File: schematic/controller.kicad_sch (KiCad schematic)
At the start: 7 parts, among them U18 74LS541, U19 74LS541

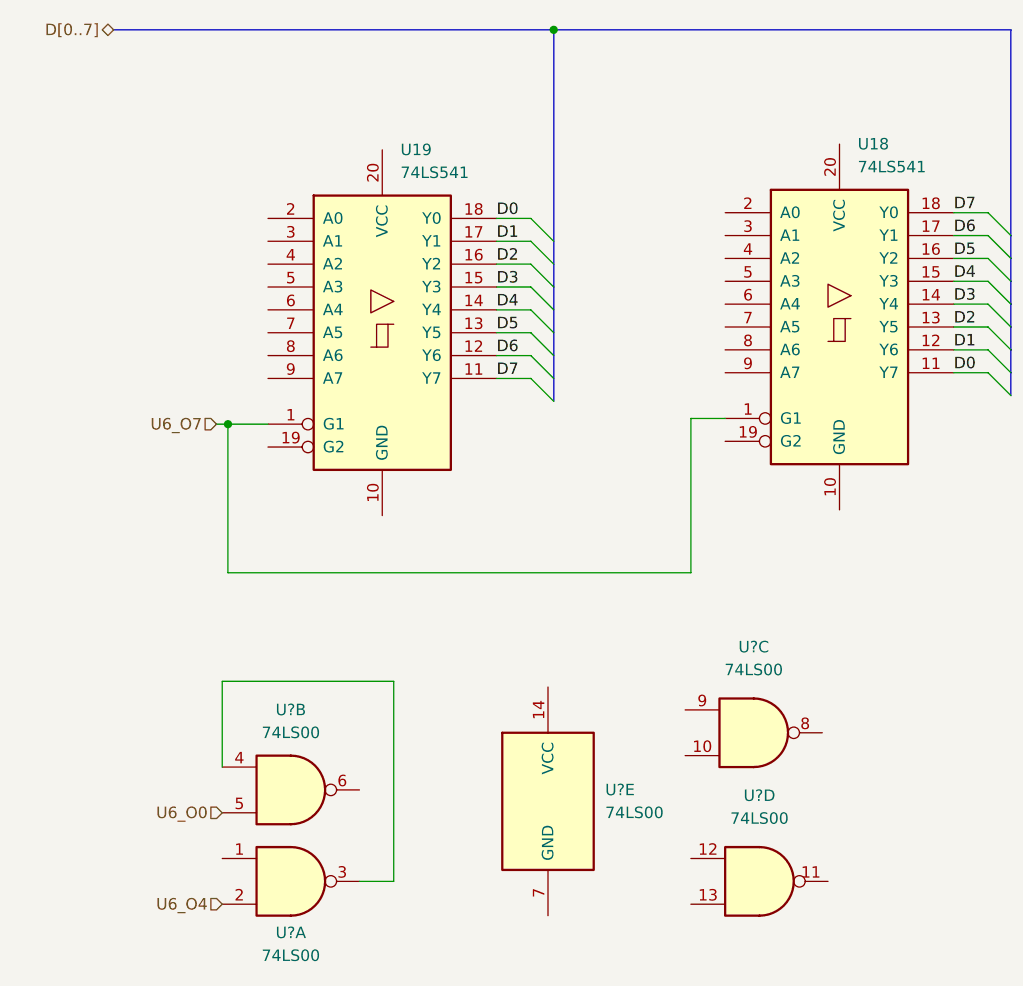
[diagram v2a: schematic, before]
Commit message: completed sound block, finished cart io port, and finished decoder.
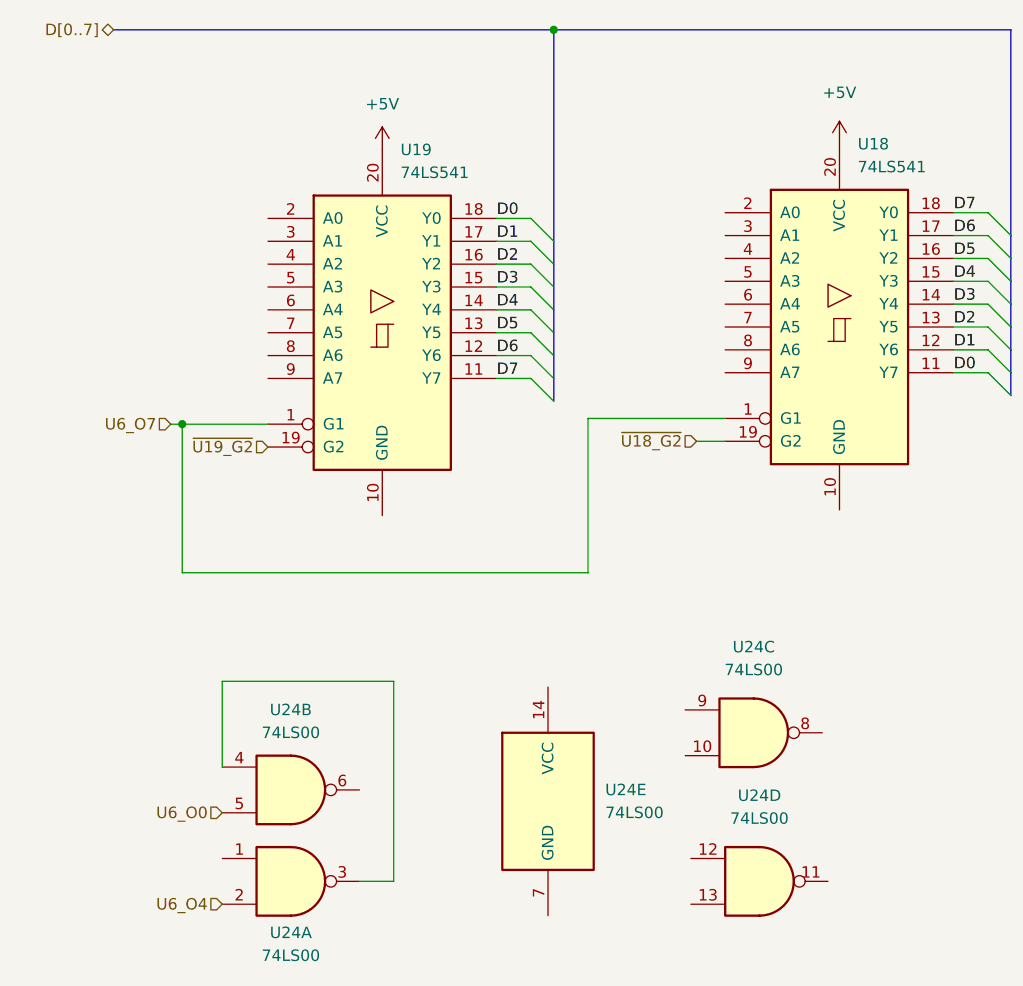
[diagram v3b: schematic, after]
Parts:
- gave numbers to parts that had none: 1
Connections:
- net ~{U19_G2}: now reaches U19.19 (G2)
- net +5V: now reaches U19.20 (VCC)
- net +5V: now also U18.20 (VCC)
- net ~{U18_G2}: now reaches U18.19 (G2)
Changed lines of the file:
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@@
 (kicad_sch (version 20211123) (generator eeschema)
   (paper "A4")
-  (junction (at 106.68 97.79) (diameter 0) (color 0 0 0 0)
+  (junction (at 101.6 97.79) (diameter 0) (color 0 0 0 0)
   )
   (junction (at 142.875 53.975) (diameter 0) (color 0 0 0 0)
@@
     (stroke (width 0) (type default) (color 0 0 0 0))
   )
-  (wire (pts (xy 106.68 97.79) (xy 106.68 114.3))
+  (wire (pts (xy 101.6 97.79) (xy 101.6 114.3))
     (stroke (width 0) (type default) (color 0 0 0 0))
   )
@@
     (stroke (width 0) (type default) (color 0 0 0 0))
   )
-  (wire (pts (xy 106.68 97.79) (xy 111.125 97.79))
+  (wire (pts (xy 101.6 97.79) (xy 111.125 97.79))
+    (stroke (width 0) (type default) (color 0 0 0 0))
+  )
+  (wire (pts (xy 158.75 99.695) (xy 161.925 99.695))
     (stroke (width 0) (type default) (color 0 0 0 0))
   )
@@
     (stroke (width 0) (type default) (color 0 0 0 0))
   )
-  (wire (pts (xy 106.68 114.3) (xy 158.115 114.3))
+  (wire (pts (xy 101.6 114.3) (xy 146.685 114.3))
     (stroke (width 0) (type default) (color 0 0 0 0))
   )
@@
     (stroke (width 0) (type default) (color 0 0 0 0))
   )
-  (wire (pts (xy 158.115 97.155) (xy 161.925 97.155))
+  (wire (pts (xy 146.685 97.155) (xy 161.925 97.155))
     (stroke (width 0) (type default) (color 0 0 0 0))
   )
@@
     (stroke (width 0) (type default) (color 0 0 0 0))
   )
-  (wire (pts (xy 105.41 97.79) (xy 106.68 97.79))
+  (wire (pts (xy 100.33 97.79) (xy 101.6 97.79))
     (stroke (width 0) (type default) (color 0 0 0 0))
   )
@@
     (stroke (width 0) (type default) (color 0 0 0 0))
   )
-  (wire (pts (xy 158.115 114.3) (xy 158.115 97.155))
+  (wire (pts (xy 146.685 114.3) (xy 146.685 97.155))
     (stroke (width 0) (type default) (color 0 0 0 0))
   )
@@
     (effects (font (size 1.27 1.27)) (justify right))
   )
-  (hierarchical_label "U6_O7" (shape input) (at 105.41 97.79 180)
+  (hierarchical_label "U6_O7" (shape input) (at 100.33 97.79 180)
+    (effects (font (size 1.27 1.27)) (justify right))
+  )
+  (hierarchical_label "~{U19_G2}" (shape input) (at 111.125 100.33 180)
     (effects (font (size 1.27 1.27)) (justify right))
   )
   (hierarchical_label "D[0..7]" (shape bidirectional) (at 93.98 53.975 180)
+    (effects (font (size 1.27 1.27)) (justify right))
+  )
+  (hierarchical_label "~{U18_G2}" (shape input) (at 158.75 99.695 180)
     (effects (font (size 1.27 1.27)) (justify right))
   )
@@
   (symbol (lib_id "74xx:74LS00") (at 165.735 148.59 0) (unit 4)
     (in_bom yes) (on_board yes) (fields_autoplaced)
-    (property "Reference" "U?" (id 0) (at 165.735 139.065 0))
+    (property "Reference" "U24" (id 0) (at 165.735 139.065 0))
     (property "Value" "74LS00" (id 1) (at 165.735 141.605 0))
     (property "Footprint" "" (id 2) (at 165.735 148.59 0)
@@
   (symbol (lib_id "74xx:74LS00") (at 142.24 139.7 0) (unit 5)
     (in_bom yes) (on_board yes) (fields_autoplaced)
-    (property "Reference" "U?" (id 0) (at 148.59 138.4299 0)
+    (property "Reference" "U24" (id 0) (at 148.59 138.4299 0)
       (effects (font (size 1.27 1.27)) (justify left))
     )
@@
     (pin "7")
   )
+  (symbol (lib_id "power:+5V") (at 123.825 67.31 0) (unit 1)
+    (in_bom yes) (on_board yes) (fields_autoplaced)
+    (property "Reference" "#PWR?" (id 0) (at 123.825 71.12 0)
+      (effects (font (size 1.27 1.27)) hide)
+    )
+    (property "Value" "+5V" (id 1) (at 123.825 62.23 0))
+    (property "Footprint" "" (id 2) (at 123.825 67.31 0)
+      (effects (font (size 1.27 1.27)) hide)
+    )
+    (property "Datasheet" "" (id 3) (at 123.825 67.31 0)
+      (effects (font (size 1.27 1.27)) hide)
+    )
+    (pin "1")
+  )
   (symbol (lib_id "74xx:74LS00") (at 165.1 132.08 0) (unit 3)
     (in_bom yes) (on_board yes) (fields_autoplaced)
-    (property "Reference" "U?" (id 0) (at 165.1 122.555 0))
+    (property "Reference" "U24" (id 0) (at 165.1 122.555 0))
     (property "Value" "74LS00" (id 1) (at 165.1 125.095 0))
     (property "Footprint" "" (id 2) (at 165.1 132.08 0)
@@
     (pin "7")
   )
+  (symbol (lib_id "power:+5V") (at 174.625 66.675 0) (unit 1)
+    (in_bom yes) (on_board yes) (fields_autoplaced)
+    (property "Reference" "#PWR?" (id 0) (at 174.625 70.485 0)
+      (effects (font (size 1.27 1.27)) hide)
+    )
+    (property "Value" "+5V" (id 1) (at 174.625 60.96 0))
+    (property "Footprint" "" (id 2) (at 174.625 66.675 0)
+      (effects (font (size 1.27 1.27)) hide)
+    )
+    (property "Datasheet" "" (id 3) (at 174.625 66.675 0)
+      (effects (font (size 1.27 1.27)) hide)
+    )
+    (pin "1")
+  )
   (symbol (lib_id "74xx:74LS00") (at 113.665 148.59 0) (unit 1)
     (in_bom yes) (on_board yes)
-    (property "Reference" "U?" (id 0) (at 113.665 154.305 0))
+    (property "Reference" "U24" (id 0) (at 113.665 154.305 0))
     (property "Value" "74LS00" (id 1) (at 113.665 156.845 0))
     (property "Footprint" "" (id 2) (at 113.665 148.59 0)
@@
   (symbol (lib_id "74xx:74LS00") (at 113.665 138.43 0) (unit 2)
     (in_bom yes) (on_board yes) (fields_autoplaced)
-    (property "Reference" "U?" (id 0) (at 113.665 129.54 0))
+    (property "Reference" "U24" (id 0) (at 113.665 129.54 0))
     (property "Value" "74LS00" (id 1) (at 113.665 132.08 0))
     (property "Footprint" "" (id 2) (at 113.665 138.43 0)

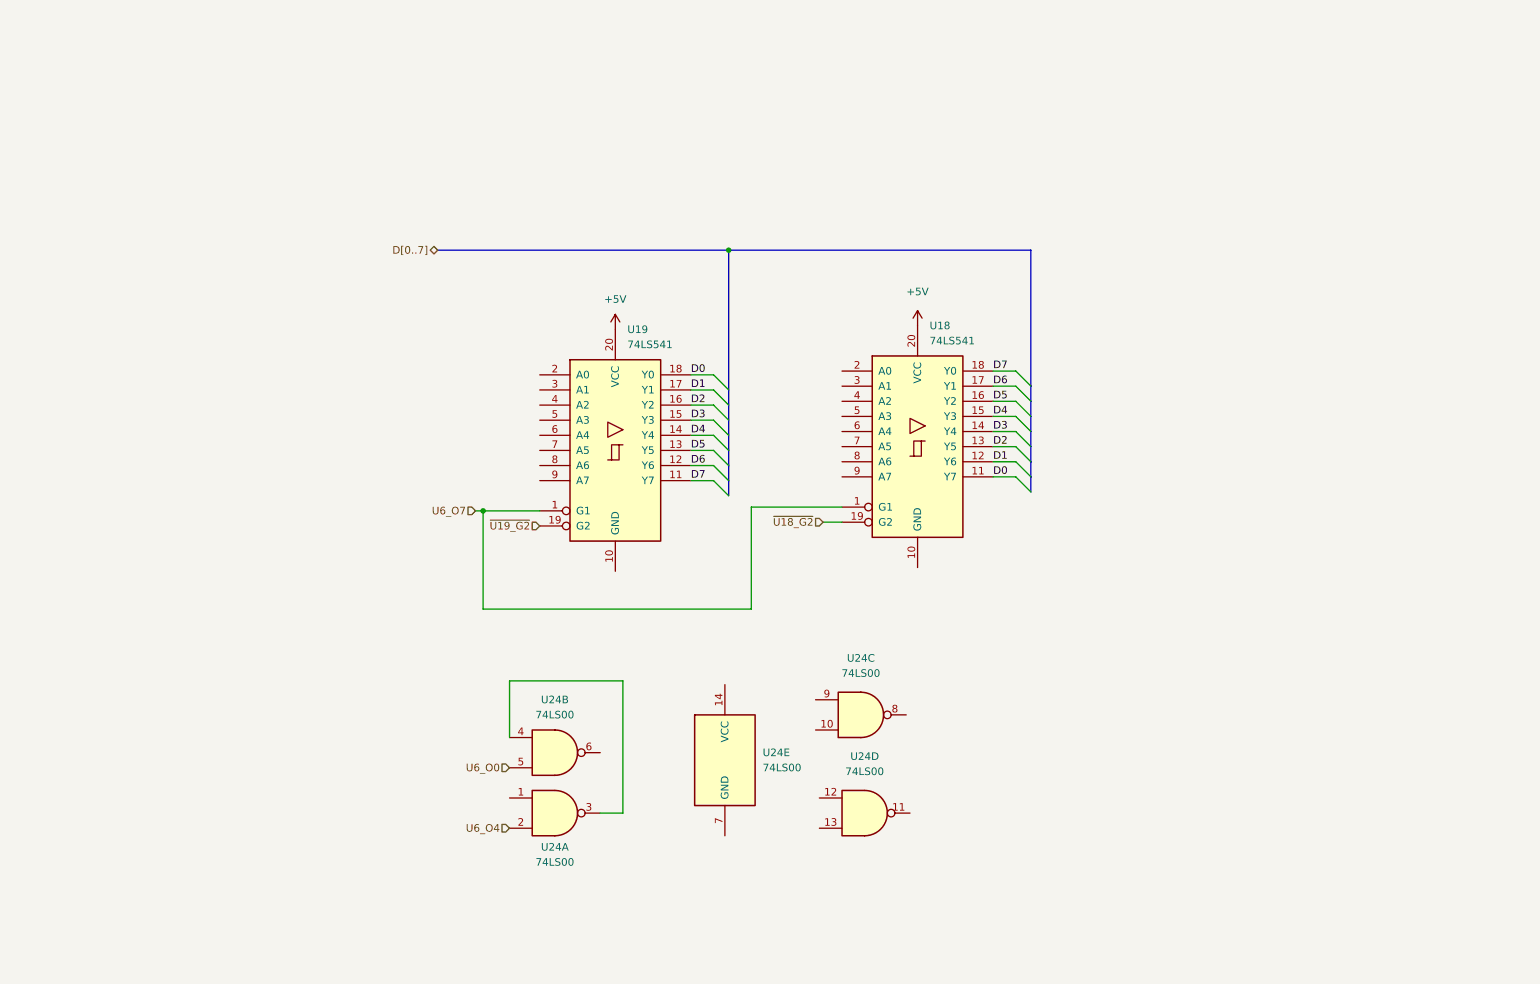
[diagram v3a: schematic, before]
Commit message: power supply added, controller circuit added. Controller is a very odd duck to say the least. Seems they wanted to have plenty of current, maybe due to the steering wheel attachement?
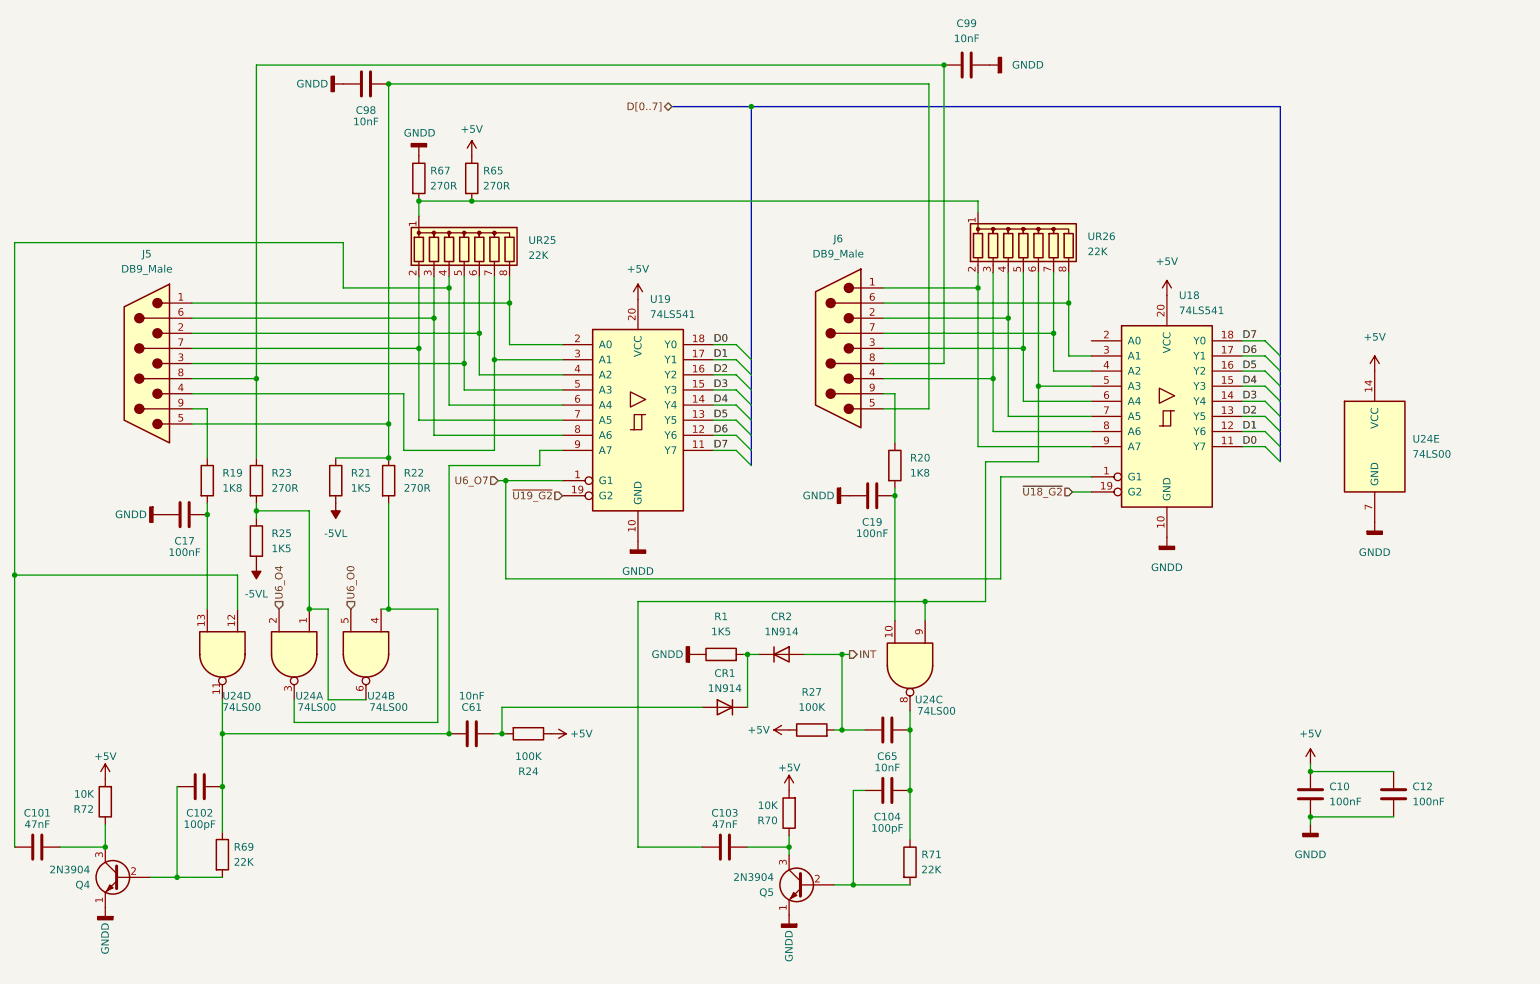
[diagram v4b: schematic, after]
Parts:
- added C10, C12, C17, C19: 100nF, symbol Device:C
- added C101, C103: 47nF, symbol Device:C
- added C102, C104: 100pF, symbol Device:C
- added C61, C65, C98, C99: 10nF, symbol Device:C
- added CR1, CR2: 1N914, symbol Device:D
- added J5, J6: DB9_Male, symbol Connector:DB9_Male
- added Q4, Q5: 2N3904, Package_TO_SOT_THT:TO-92_Inline, symbol Transistor_BJT:2N3904
- added R1, R21, R25: 1K5, symbol Device:R
- added R19, R20: 1K8, symbol Device:R
- added R22, R23, R65, R67: 270R, symbol Device:R
- added R24, R27: 100K, symbol Device:R
- added R69, R71: 22K, symbol Device:R
- added R70, R72: 10K, symbol Device:R
- added UR25, UR26: 22K, Resistor_THT:R_Array_SIP8, symbol Device:R_Network07
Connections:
- net +5V: now also U24.14 (VCC), C10.1, C12.1, R24.1, R27.1, R65.1, R70.2, R72.2
- net GNDD: now reaches U19.10 (GND)
- net GNDD: now also U18.10 (GND), U24.7 (GND), C10.2, C12.2, C17.1, C19.1, C98.1, C99.2, Q4.1 (E), Q5.1 (E), R1.1, R67.1
- net at U19.2 (A0): now also J5.1, UR25.8 (R7)
- net at U19.3 (A1): now also J5.4, UR25.7 (R6)
- net at U19.4 (A2): now also J5.2, UR25.6 (R5)
- net at U19.5 (A3): now also J5.3, UR25.5 (R4)
- net at U19.6 (A4): now also U24.12, C101.2, UR25.4 (R3)
- net at U19.7 (A5): now also J5.7, UR25.2 (R1)
- net at U19.8 (A6): now also J5.6, UR25.3 (R2)
- net at U19.9 (A7): now also U24.11, C102.2, C61.2, R69.1
- net at U24.13: now also C17.2, R19.2
- net at U18.3 (A1): now also J6.6, UR26.8 (R7)
- net at U18.4 (A2): now also J6.7, UR26.7 (R6)
- net at U18.5 (A3): now also U24.9, C103.2, UR26.6 (R5)
- net at U18.6 (A4): now also J6.3, UR26.5 (R4)
- net at U18.7 (A5): now also J6.2, UR26.4 (R3)
- net at U18.8 (A6): now also J6.4, UR26.3 (R2)
- net at U18.9 (A7): now also J6.1, UR26.2 (R1)
- net at U24.10: now also C19.2, R20.2
- net at U24.8: now also C104.2, C65.2, R71.1
- net at U24.1: now also U24.6, R23.2, R25.1
- net at U24.3, U24.4: now also R22.2
- new net: CR1.1 (K), CR2.1 (K), R1.2
- new net: R65.2, R67.2, UR25.1 (common), UR26.1 (common)
- new net: C102.1, Q4.2 (B), R69.2
- new net: C101.1, Q4.3 (C), R72.1
- new net: C98.2, J5.5, J6.5, R21.1, R22.1
- new net: C61.1, CR1.2 (A), R24.2
- new net: C99.1, J5.8, J6.8, R23.1
- new net: C104.1, Q5.2 (B), R71.2
- new net: C103.1, Q5.3 (C), R70.1
- new net: J5.9, R19.1
- new net: J6.9, R20.1
- new net -5VL: R21.2, R25.2
- new net INT: C65.1, CR2.2 (A), R27.2
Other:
- moved on the sheet: U18, U19, U24A, U24B, U24C, U24D, U24E

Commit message: started work on clock_reset_misc circuits. inverter u7 done, u8 added and starting work around U22.
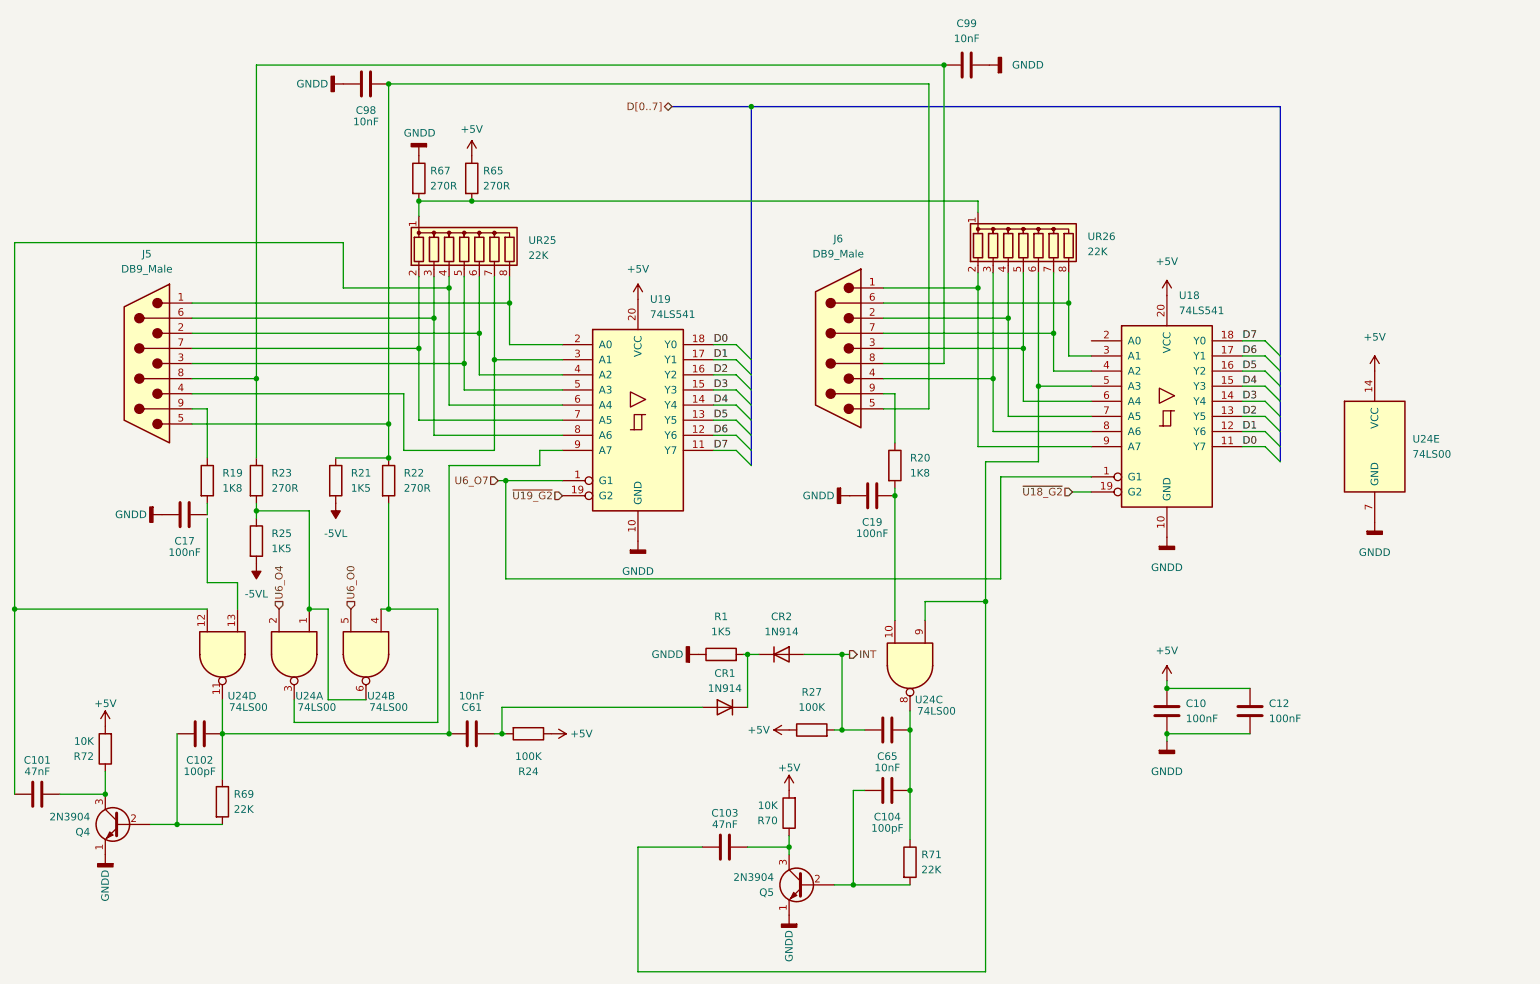
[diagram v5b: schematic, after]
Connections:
- net at C17.2, R19.2: no longer U24.13
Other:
- moved on the sheet: C10, C101, C102, C12, Q4, R69, R72, U24D
